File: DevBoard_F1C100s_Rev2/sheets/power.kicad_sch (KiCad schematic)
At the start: 39 parts, among them J1 USB_C_Receptacle_USB2.0_16P, U2 TPS562201DDCT, U3 TPS562201DDCT, U4 TPS562201DDCT

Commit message: Finish schematic rev2
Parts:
- removed C14: 0.1uf, Capacitor_SMD:C_0603_1608Metric_Pad1.08x0.95mm_HandSolder, symbol Device:C_Small
- added C201, C203: 22uf, Capacitor_SMD:C_0603_1608Metric_Pad1.08x0.95mm_HandSolder, symbol Device:C_Small
- added C202: 0.1uf, Capacitor_SMD:C_0603_1608Metric_Pad1.08x0.95mm_HandSolder, symbol Device:C_Small
- added D201: 1N5819WS, Diode_SMD:D_SOD-523, symbol Diode:1N5819WS
- added JP201, JP202: SolderJumper_2_Open, Jumper:SolderJumper-2_P1.3mm_Open_Pad1.0x1.5mm, symbol Jumper:SolderJumper_2_Open
- added L201: 4.7uH, symbol Device:L_Small
- added R201, R202: 10R, Resistor_SMD:R_0603_1608Metric_Pad0.98x0.95mm_HandSolder, symbol Device:R_Small
- added R204: 10k, Resistor_SMD:R_0603_1608Metric_Pad0.98x0.95mm_HandSolder, symbol Device:R_Small
- added U201: AP3031KTR-G1, SOT23-6_DIO, symbol AP3031KTR_G1:AP3031KTR-G1
- R?: value 4.7k -> 2.2k
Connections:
- net 5V: now also C203.1, L201.1, R204.1, U201.6 (VIN)
- net GND: now also C201.2, C202.2, C203.2, R201.2, R202.2, U201.2 (GND)
- net VBUS: no longer names the net of F1.2, J1.A4 (VBUS), J1.A9 (VBUS), J1.B4 (VBUS), J1.B9 (VBUS)
- new net: C201.1, C202.1, D201.1 (K), JP201.1 (A), U201.5 (OV)
- new net: R204.2, U201.4 (CTRL)
- new net: JP202.1 (A), R201.1, R202.1, U201.3 (FB)
- new net: D201.2 (A), L201.2, U201.1 (SW)
- new net VLEDA: JP201.2 (B)
- new net VLEDK: JP202.2 (B)
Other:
- moved on the sheet: C13, D?, F1, J1, R4, R5, R?

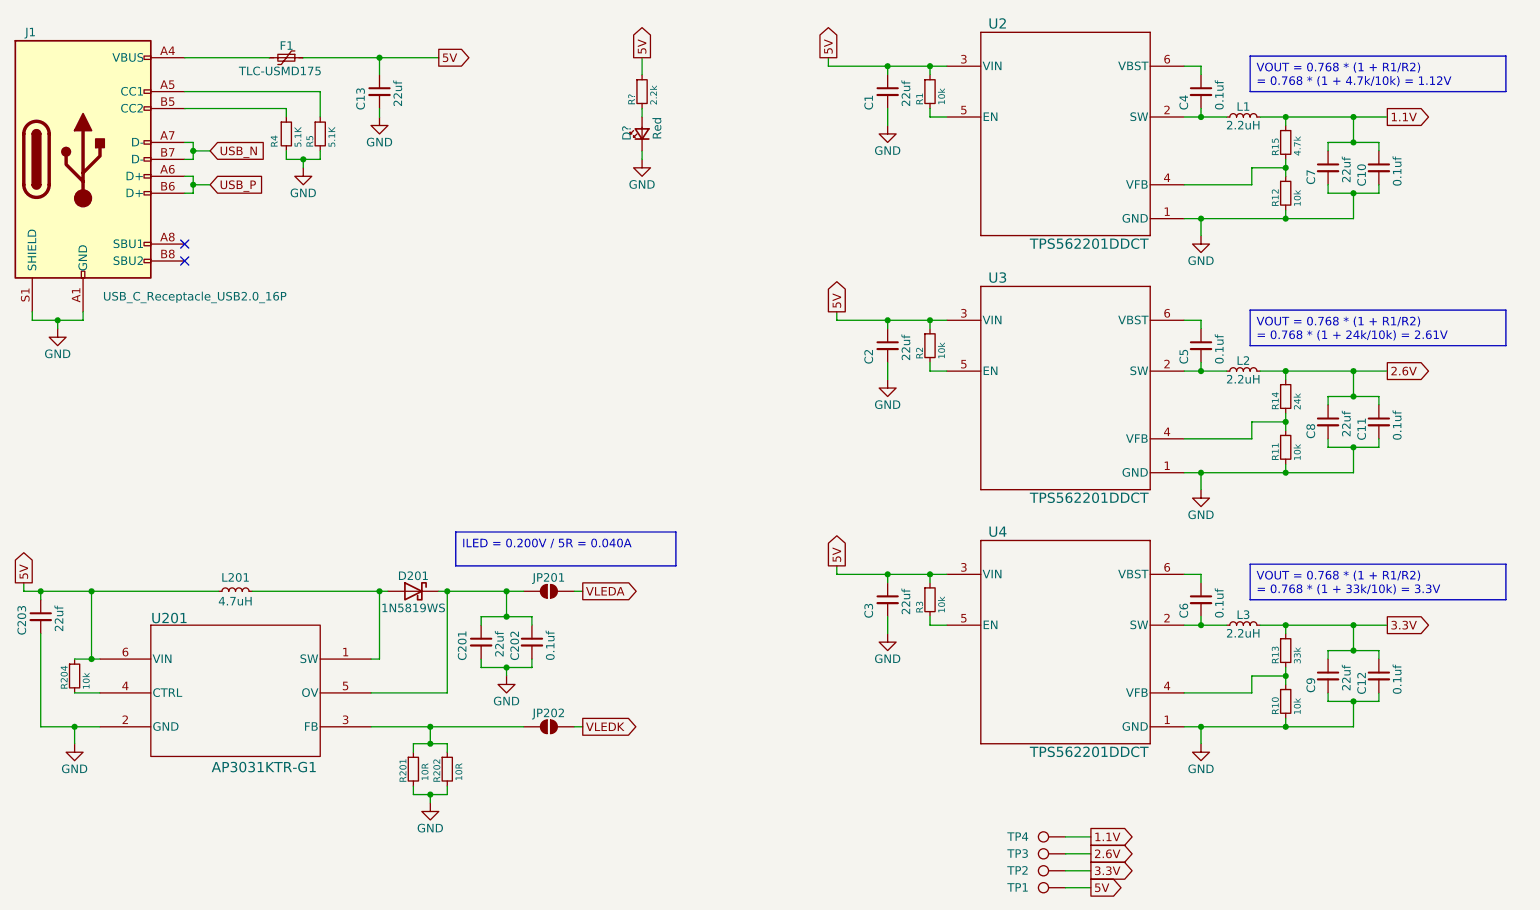
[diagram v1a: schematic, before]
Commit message: Update schematic annotations
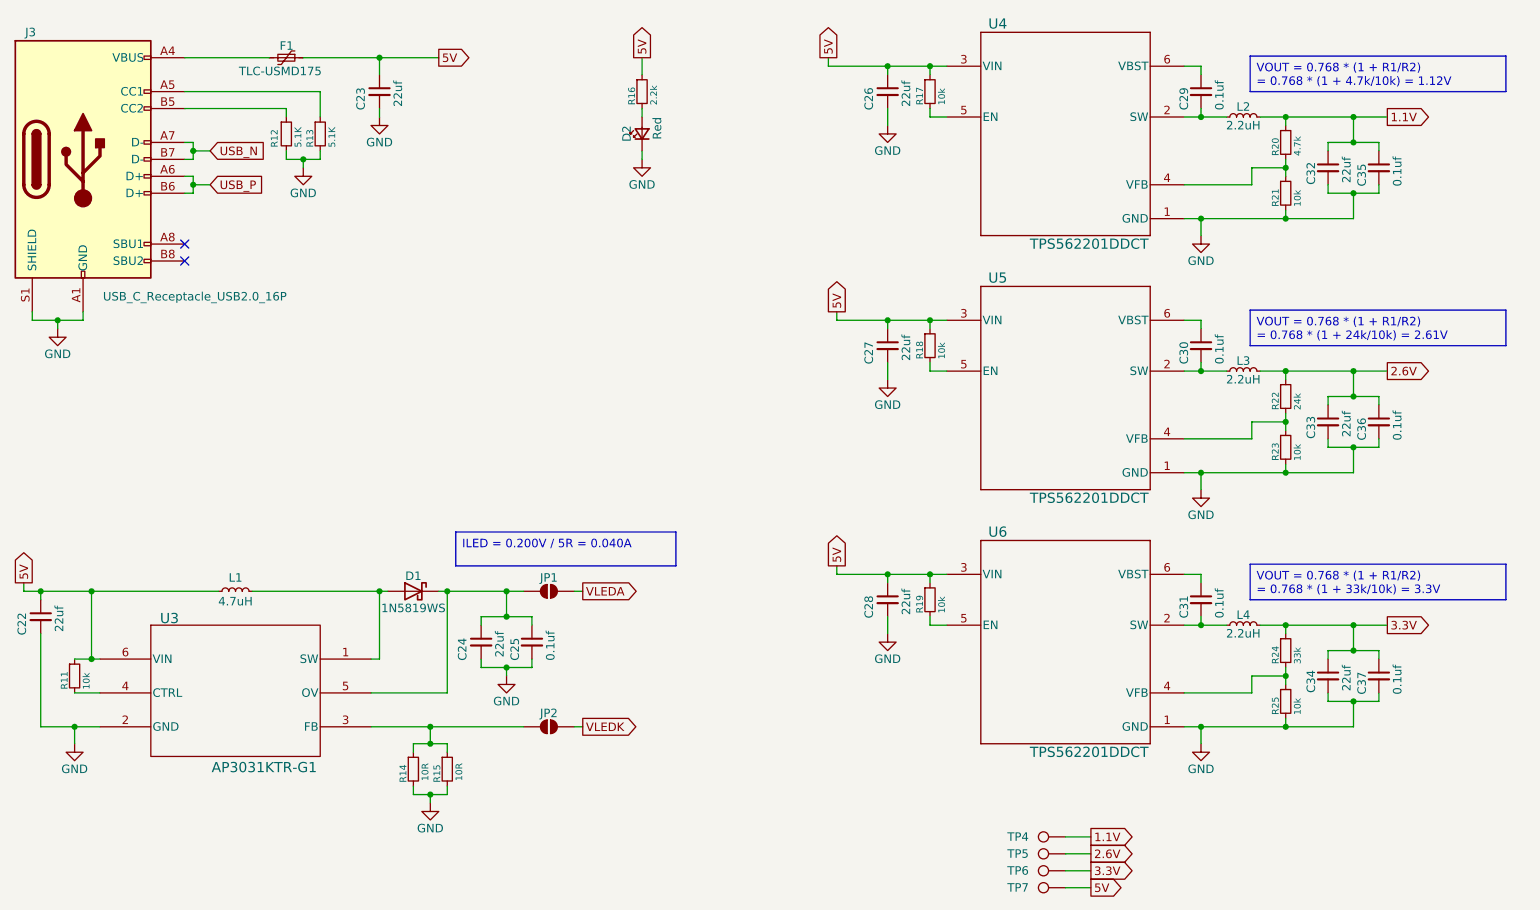
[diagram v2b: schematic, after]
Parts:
- D2: renamed from D?; footprint (none) -> LED_SMD:LED_0603_1608Metric_Pad1.05x0.95mm_HandSolder
- F1: footprint (none) -> Fuse:Fuse_1210_3225Metric_Pad1.42x2.65mm_HandSolder
- L1: renamed from L201; footprint (none) -> Inductor_SMD:L_0805_2012Metric_Pad1.15x1.40mm_HandSolder
- U3: renamed from U201; footprint SOT23-6_DIO -> AP3031KTR_G1:SOT23-6_DIO
- gave numbers to parts that had none: 1
- renumbered C203 to C22, C13 to C23, C201 to C24, C202 to C25, C1 to C26, C2 to C27, C3 to C28, C4 to C29, C5 to C30, C6 to C31, C7 to C32, C8 to C33, C9 to C34, C10 to C35, C11 to C36, C12 to C37, D201 to D1, J1 to J3, JP201 to JP1, JP202 to JP2, L1 to L2, L2 to L3, L3 to L4, R204 to R11, R4 to R12, R5 to R13, R201 to R14, R202 to R15, R1 to R17, R2 to R18, R3 to R19, R15 to R20, R12 to R21, R14 to R22, R11 to R23, R13 to R24, R10 to R25, TP3 to TP5, TP2 to TP6, TP1 to TP7, U2 to U4, U3 to U5, U4 to U6

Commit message: Update schematic and footprints
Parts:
- added U4: USBLC6-2SC6, Package_TO_SOT_SMD:SOT-23-6, symbol Power_Protection:USBLC6-2SC6
- L2, L3, L4: footprint Inductor_SMD:L_APV_ANR252012 -> Inductor_SMD:L_Sunlord_SWPA4030S
- TP7: footprint TestPoint:TestPoint_Pad_D2.0mm -> TestPoint:TestPoint_Pad_D1.0mm
- renumbered R13 to R12, R12 to R13, U4 to U5, U5 to U6, U6 to U7
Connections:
- net 5V: now also U4.5 (VBUS)
- net GND: now also U4.2 (GND)
- net USB_N: now also U4.6 (I/O1); no longer J3.A7 (D-), J3.B7 (D-)
- net USB_P: now also U4.4 (I/O2); no longer J3.A6 (D+), J3.B6 (D+)
- new net D+: J3.A6 (D+), J3.B6 (D+), U4.3 (I/O2)
- new net D-: J3.A7 (D-), J3.B7 (D-), U4.1 (I/O1)
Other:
- moved on the sheet: C23, D2, R12, R13, R16

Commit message: Finish layout
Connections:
- net VBUS: now reaches F1.2, J3.A4 (VBUS), J3.A9 (VBUS), J3.B4 (VBUS), J3.B9 (VBUS)
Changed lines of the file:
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@@
+		)
+	)
+	(label "VBUS"
+		(at 60.96 35.56 0)
+		(effects
+			(font
+				(size 1.27 1.27)
+			)
+			(justify left bottom)
 		)
 	)
